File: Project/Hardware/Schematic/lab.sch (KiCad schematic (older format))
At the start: 27 parts, among them J1 USB_B_Micro, J2 6P Male, J3 Conn_01x03_Male, U2 STM32F411RETx, U3 NCP1117-3.3_SOT223, Y1 8MHz

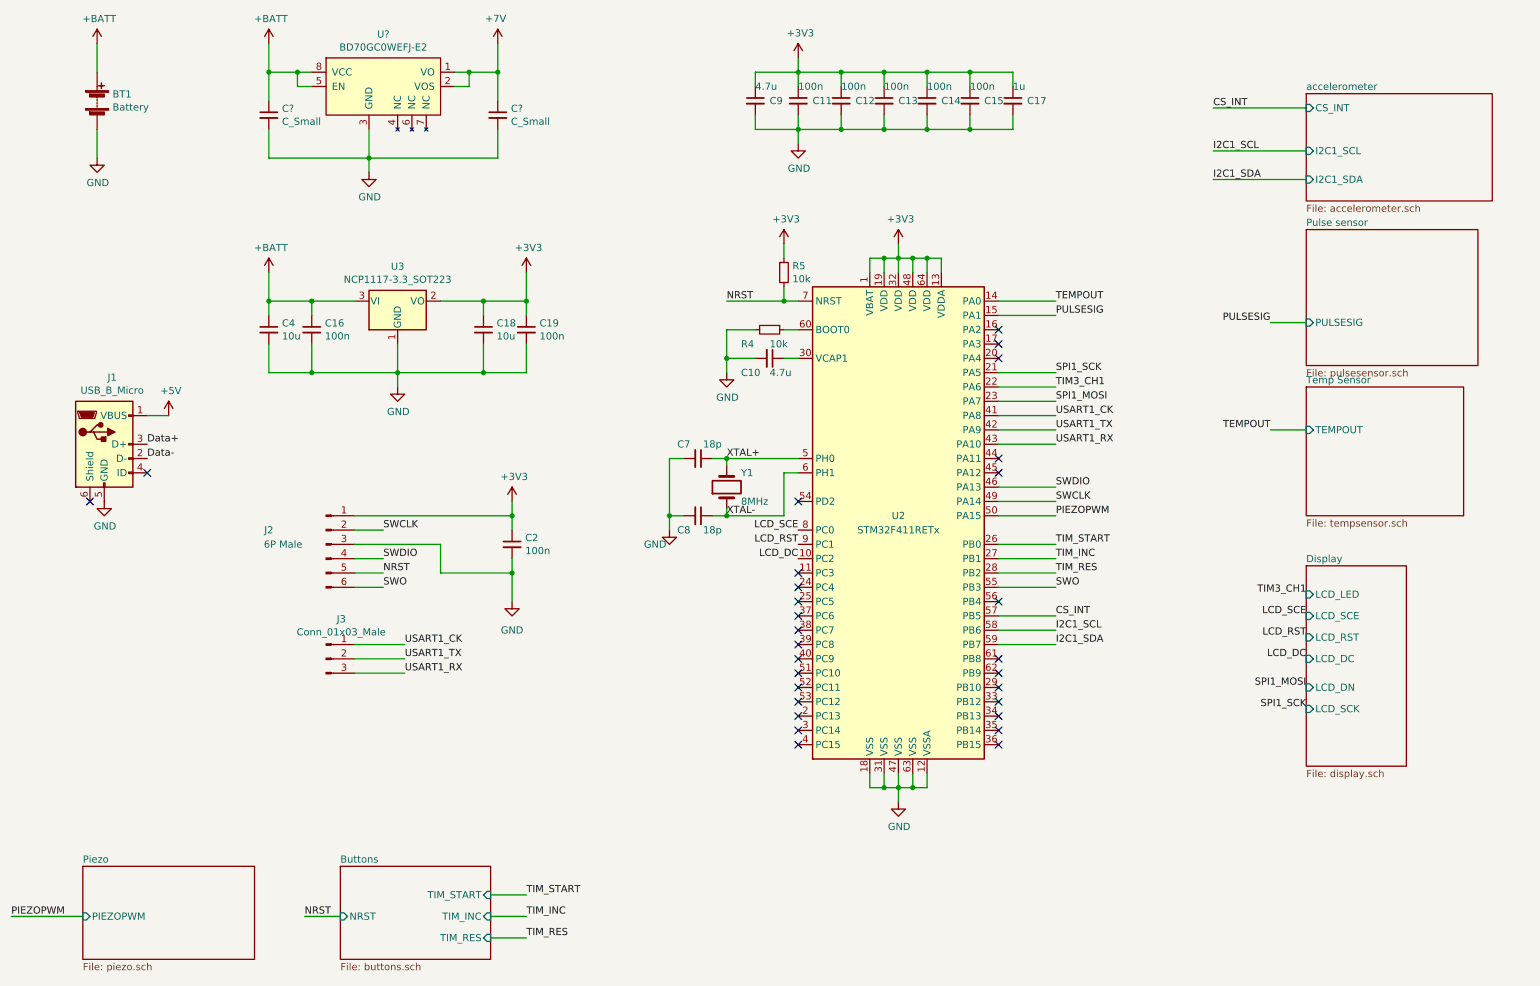
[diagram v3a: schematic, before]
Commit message: Tagit bort knapp, ändrat power till piezo
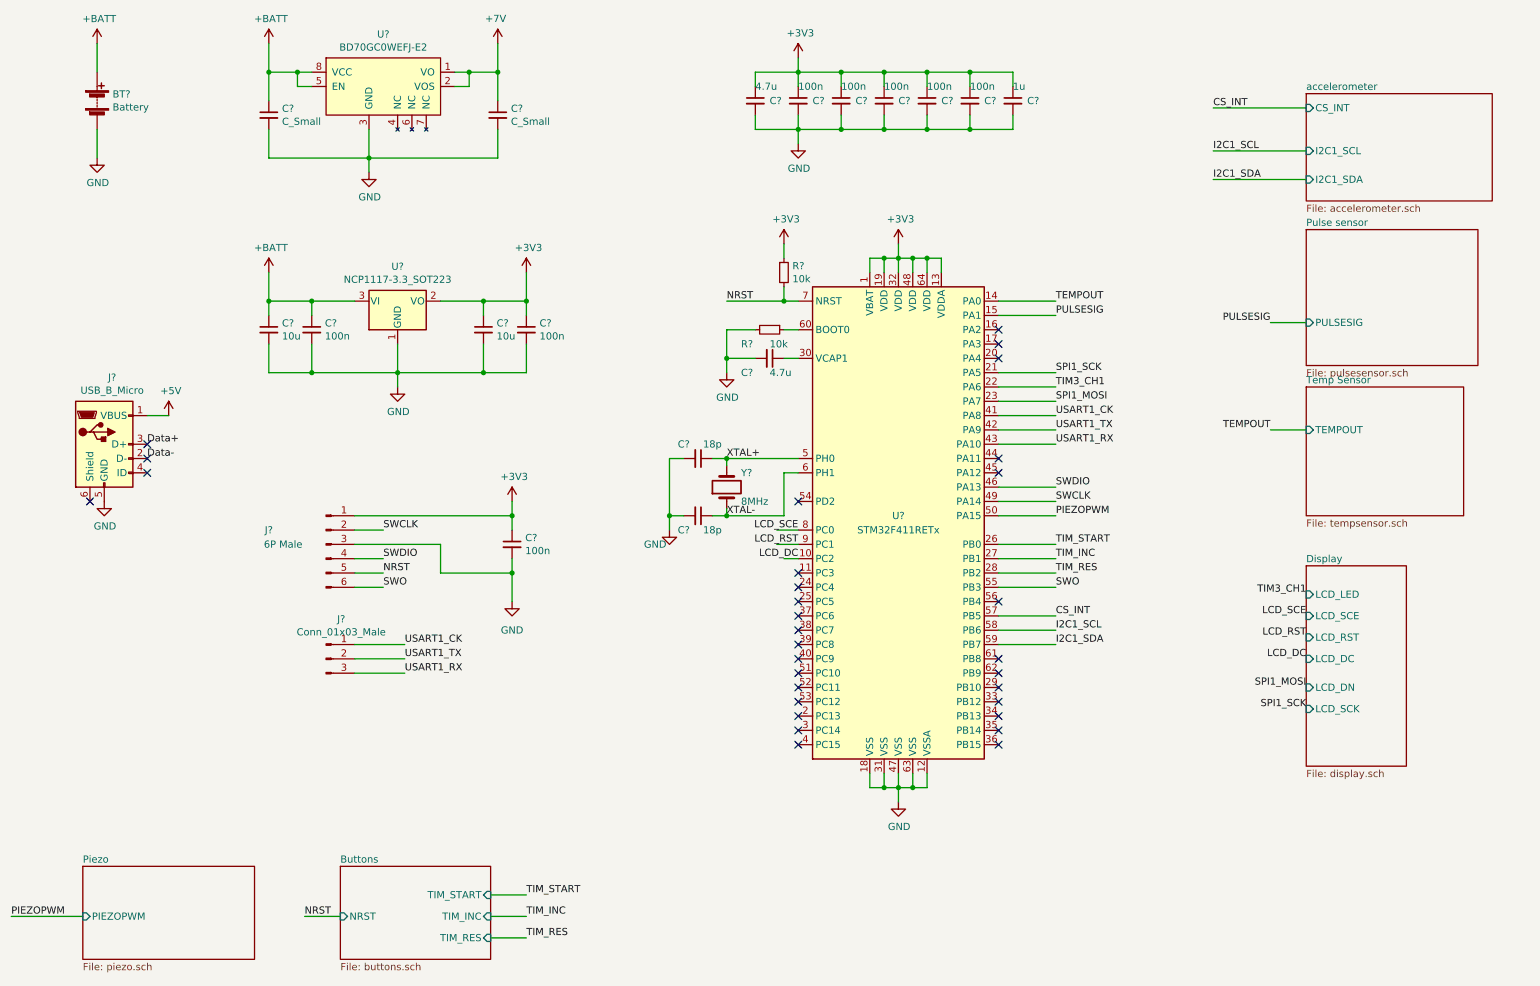
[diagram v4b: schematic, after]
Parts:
- renumbered BT1 to BT?, C12 to C?, C13 to C?, C14 to C?, C15 to C?, C11 to C?, C9 to C?, C10 to C?, C7 to C?, C8 to C?, C2 to C?, C4 to C?, C18 to C?, C19 to C?, C16 to C?, C17 to C?, J2 to J?, J3 to J?, J1 to J?, R5 to R?, R4 to R?, U2 to U?, U3 to U?, Y1 to Y?
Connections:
- no-connect marks 29 -> 31

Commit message: Tog bort power supply +7, lade till switch för att switcha mellan batteri och USB power. Lade till power-net symbol för oregulerad supply voltage +VIN.
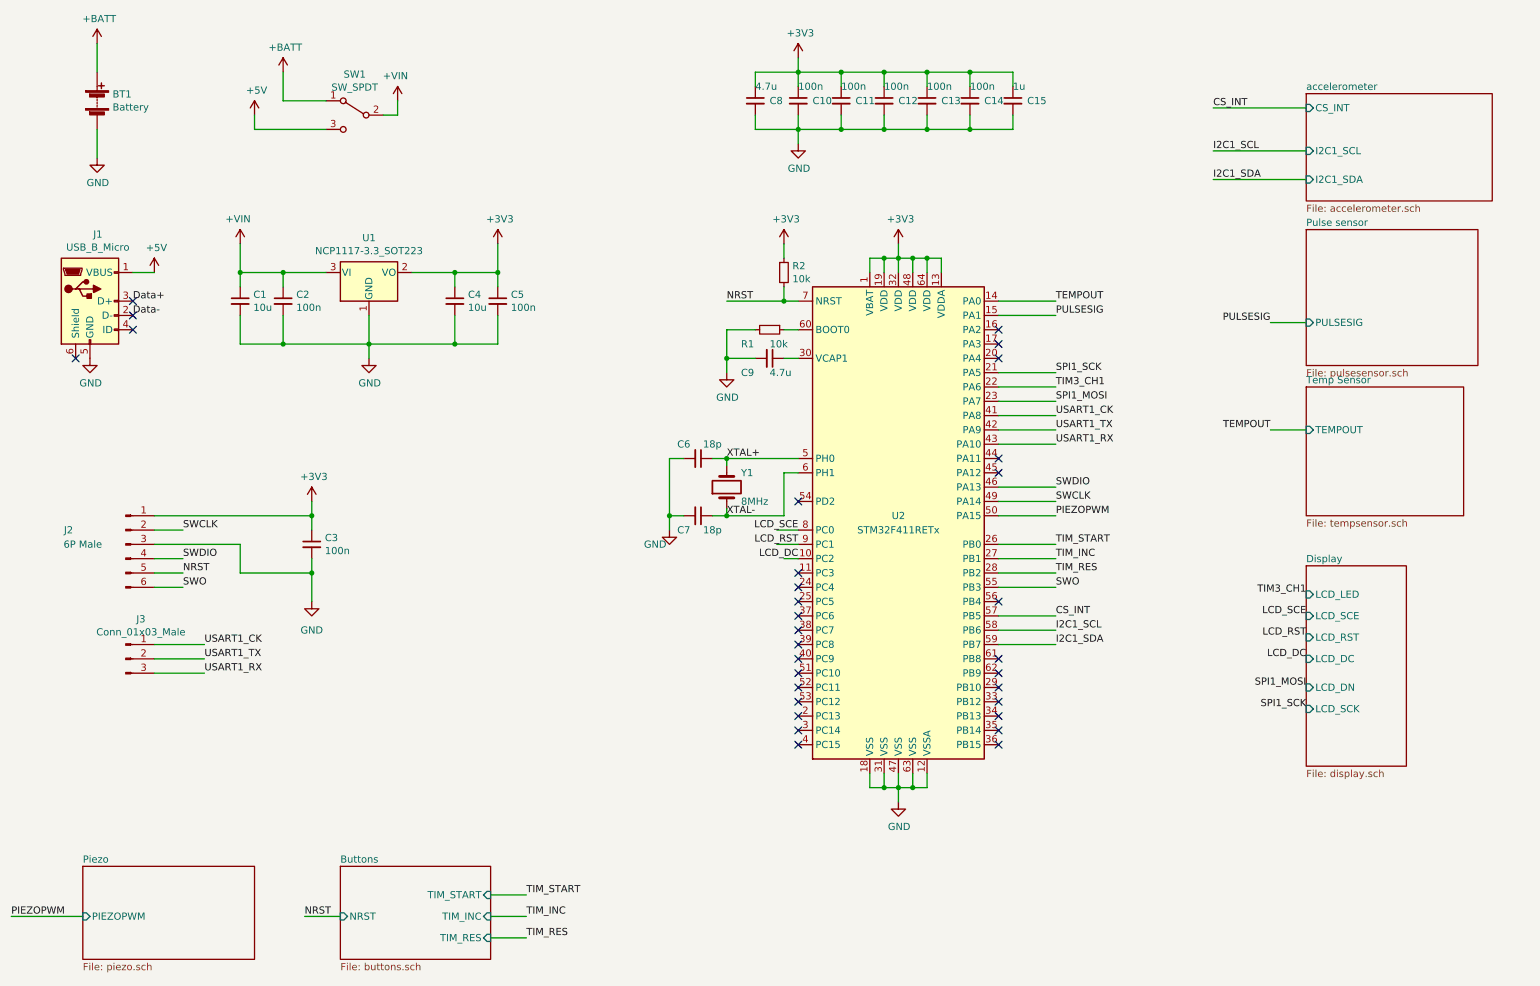
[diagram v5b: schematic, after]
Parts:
- removed C? (x2): C_Small, symbol Device:C_Small
- removed U?: BD70GC0WEFJ-E2, symbol PASC:BD70GC0WEFJ-E2
- added SW1: SW_SPDT, symbol Switch:SW_SPDT
- gave numbers to parts that had none: 24
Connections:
- net +5V: now also SW1.3 (C)
- net +BATT: now also SW1.1 (A); no longer C1.1, C2.1, U1.3 (VI)
- new net +VIN: C1.1, C2.1, SW1.2 (B), U1.3 (VI)
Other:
- moved on the sheet: C1, C2, C3, C4, C5, J1, J2, J3, U1

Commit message: Intermediate...
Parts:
- BT1: footprint (none) -> Connector_PinHeader_2.54mm:PinHeader_1x02_P2.54mm_Vertical
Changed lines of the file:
@@
 encoding utf-8
 Sheet 1 7
-Title ""
-Date ""
-Rev ""
-Comp ""
+Title "Main sheet"
+Date "2019-02-12"
+Rev "1"
+Comp "PASC"
 Comment1 ""
 Comment2 ""
@@
 F 0 "BT1" H 1308 1346 50  0000 L CNN
 F 1 "Battery" H 1308 1255 50  0000 L CNN
-F 2 "" V 1200 1360 50  0001 C CNN
+F 2 "Connector_PinHeader_2.54mm:PinHeader_1x02_P2.54mm_Vertical" V 1200 1360 50  0001 C CNN
 F 3 "~" V 1200 1360 50  0001 C CNN
 	1    1200 1300

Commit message: Lade till vippströmställare footprint och uppdaterade max4460 footprint för att det förhoppningsvis ska laddas av alla
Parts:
- SW1: footprint (none) -> PASC:100-SP1-T100B3M1QE
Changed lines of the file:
@@
 F 0 "SW1" H 3000 1685 50  0000 C CNN
 F 1 "SW_SPDT" H 3000 1594 50  0000 C CNN
-F 2 "" H 3000 1400 50  0001 C CNN
+F 2 "PASC:100-SP1-T100B3M1QE" H 3000 1400 50  0001 C CNN
 F 3 "" H 3000 1400 50  0001 C CNN
 	1    3000 1400
